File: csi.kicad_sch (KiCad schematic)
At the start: 18 parts, among them J8 Conn_FFC_WE_68712614522_ONE-S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, U11 AP22615A_TSOT26, U12 AP22615A_TSOT26

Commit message: [#54617] Review requested changes
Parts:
- U11, U12: MPN AP22615AWU-7 -> AP22615AWU-7
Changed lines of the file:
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@@
       (effects (font (size 1.27 1.27) (thickness 0.15)) (justify left bottom) hide)
     )
-    (property "Datasheet" " " (at 322.58 171.45 0)
+    (property "Datasheet" "https://product.tdk.com/en/search/capacitor/ceramic/mlcc/info?part_no=C1005X6S1A105K050BC" (at 322.58 171.45 0)
       (effects (font (size 1.27 1.27) (thickness 0.15)) (justify left bottom) hide)
     )
@@
       (effects (font (size 1.27 1.27) (thickness 0.15)) (justify left bottom) hide)
     )
-    (property "Datasheet" "https://search.murata.co.jp/Ceramy/image/img/A01X/G101/ENG/GRM155R61H104KE14-01.pdf" (at 125.73 185.42 0)
+    (property "Datasheet" "https://www.murata.com/products/productdetail?partno=GRM155R61H104KE14%23" (at 125.73 185.42 0)
       (effects (font (size 1.27 1.27) (thickness 0.15)) (justify left bottom) hide)
     )
@@
   (symbol (lib_id "antmicropower:GND") (at 110.49 127 0) (mirror y) (unit 1)
     (in_bom yes) (on_board yes) (dnp no)
-    (property "Reference" "#PWR?" (at 110.49 133.35 0)
+    (property "Reference" "#PWR0217" (at 110.49 133.35 0)
       (effects (font (size 1.27 1.27)) (justify left bottom) hide)
     )
@@
       (project "cm4-baseboard"
         (path "/60b842dc-0853-4a25-99ac-5784ddf94d0d/49e0afda-d892-4d16-b8c1-dc5863c48dfa"
-          (reference "#PWR?") (unit 1)
+          (reference "#PWR0217") (unit 1)
         )
       )
@@
       (effects (font (size 1.27 1.27) (thickness 0.15)) (justify left bottom) hide)
     )
-    (property "Datasheet" "https://search.murata.co.jp/Ceramy/image/img/A01X/G101/ENG/GRM155R61H104KE14-01.pdf" (at 125.73 140.97 0)
+    (property "Datasheet" "https://www.murata.com/products/productdetail?partno=GRM155R61H104KE14%23" (at 125.73 140.97 0)
       (effects (font (size 1.27 1.27) (thickness 0.15)) (justify left bottom) hide)
     )
@@
   (symbol (lib_id "antmicropower:GND") (at 110.49 171.45 0) (mirror y) (unit 1)
     (in_bom yes) (on_board yes) (dnp no)
-    (property "Reference" "#PWR?" (at 110.49 177.8 0)
+    (property "Reference" "#PWR0215" (at 110.49 177.8 0)
       (effects (font (size 1.27 1.27)) (justify left bottom) hide)
     )
@@
       (project "cm4-baseboard"
         (path "/60b842dc-0853-4a25-99ac-5784ddf94d0d/49e0afda-d892-4d16-b8c1-dc5863c48dfa"
-          (reference "#PWR?") (unit 1)
+          (reference "#PWR0215") (unit 1)
         )
       )
@@
       (effects (font (size 1.27 1.27) (thickness 0.15)) (justify left bottom) hide)
     )
-    (property "Datasheet" " " (at 314.96 171.45 0)
+    (property "Datasheet" "https://product.tdk.com/en/search/capacitor/ceramic/mlcc/info?part_no=C1005X6S1A105K050BC" (at 314.96 171.45 0)
       (effects (font (size 1.27 1.27) (thickness 0.15)) (justify left bottom) hide)
     )
@@
       (effects (font (size 1.27 1.27) (thickness 0.15)) (justify left bottom) hide)
     )
-    (property "Datasheet" "https://www.mouser.pl/datasheet/2/115/DIOD_S_A0008958405_1-2543193.pdf" (at 152.4 139.7 0)
-      (effects (font (size 1.27 1.27) (thickness 0.15)) (justify left bottom) hide)
-    )
-    (property "MPN" "AP22615AWU-7 " (at 129.54 125.73 0)
+    (property "Datasheet" "https://www.mouser.com/datasheet/2/115/DIOD_S_A0008958405_1-2543193.pdf" (at 152.4 139.7 0)
+      (effects (font (size 1.27 1.27) (thickness 0.15)) (justify left bottom) hide)
+    )
+    (property "MPN" "AP22615AWU-7" (at 129.54 125.73 0)
       (effects (font (size 1.27 1.27) (thickness 0.15)))
     )
@@
   (symbol (lib_id "antmicropower:+3V3") (at 110.49 162.56 0) (unit 1)
     (in_bom yes) (on_board yes) (dnp no)
-    (property "Reference" "#PWR?" (at 110.49 166.37 0)
+    (property "Reference" "#PWR0216" (at 110.49 166.37 0)
       (effects (font (size 1.27 1.27)) (justify left bottom) hide)
     )
@@
       (effects (font (size 1.27 1.27)) hide)
     )
-    (pin "1")
-    (instances
-      (project "cm4-baseboard"
-        (path "/60b842dc-0853-4a25-99ac-5784ddf94d0d/49e0afda-d892-4d16-b8c1-dc5863c48dfa"
-          (reference "#PWR?") (unit 1)
+    (property "Author" "Antmicro" (at 125.73 165.1 0)
+      (effects (font (size 1.27 1.27) (thickness 0.15)) (justify left bottom) hide)
+    )
+    (property "License" "Apache-2.0" (at 125.73 167.64 0)
+      (effects (font (size 1.27 1.27) (thickness 0.15)) (justify left bottom) hide)
+    )
+    (pin "1")
+    (instances
+      (project "cm4-baseboard"
+        (path "/60b842dc-0853-4a25-99ac-5784ddf94d0d/49e0afda-d892-4d16-b8c1-dc5863c48dfa"
+          (reference "#PWR0216") (unit 1)
         )
       )
@@
       (effects (font (size 1.27 1.27) (thickness 0.15)) (justify left bottom) hide)
     )
-    (property "Datasheet" "https://www.mouser.pl/datasheet/2/115/DIOD_S_A0008958405_1-2543193.pdf" (at 152.4 184.15 0)
-      (effects (font (size 1.27 1.27) (thickness 0.15)) (justify left bottom) hide)
-    )
-    (property "MPN" "AP22615AWU-7 " (at 129.54 170.18 0)
+    (property "Datasheet" "https://www.mouser.com/datasheet/2/115/DIOD_S_A0008958405_1-2543193.pdf" (at 152.4 184.15 0)
+      (effects (font (size 1.27 1.27) (thickness 0.15)) (justify left bottom) hide)
+    )
+    (property "MPN" "AP22615AWU-7" (at 129.54 170.18 0)
       (effects (font (size 1.27 1.27) (thickness 0.15)))
     )
@@
       (effects (font (size 1.27 1.27)) hide)
     )
-    (pin "1")
+    (property "Author" "Antmicro" (at 125.73 125.73 0)
+      (effects (font (size 1.27 1.27) (thickness 0.15)) (justify left bottom) hide)
+    )
+    (property "License" "Apache-2.0" (at 125.73 128.27 0)
+      (effects (font (size 1.27 1.27) (thickness 0.15)) (justify left bottom) hide)
+    )
+    (pin "1")

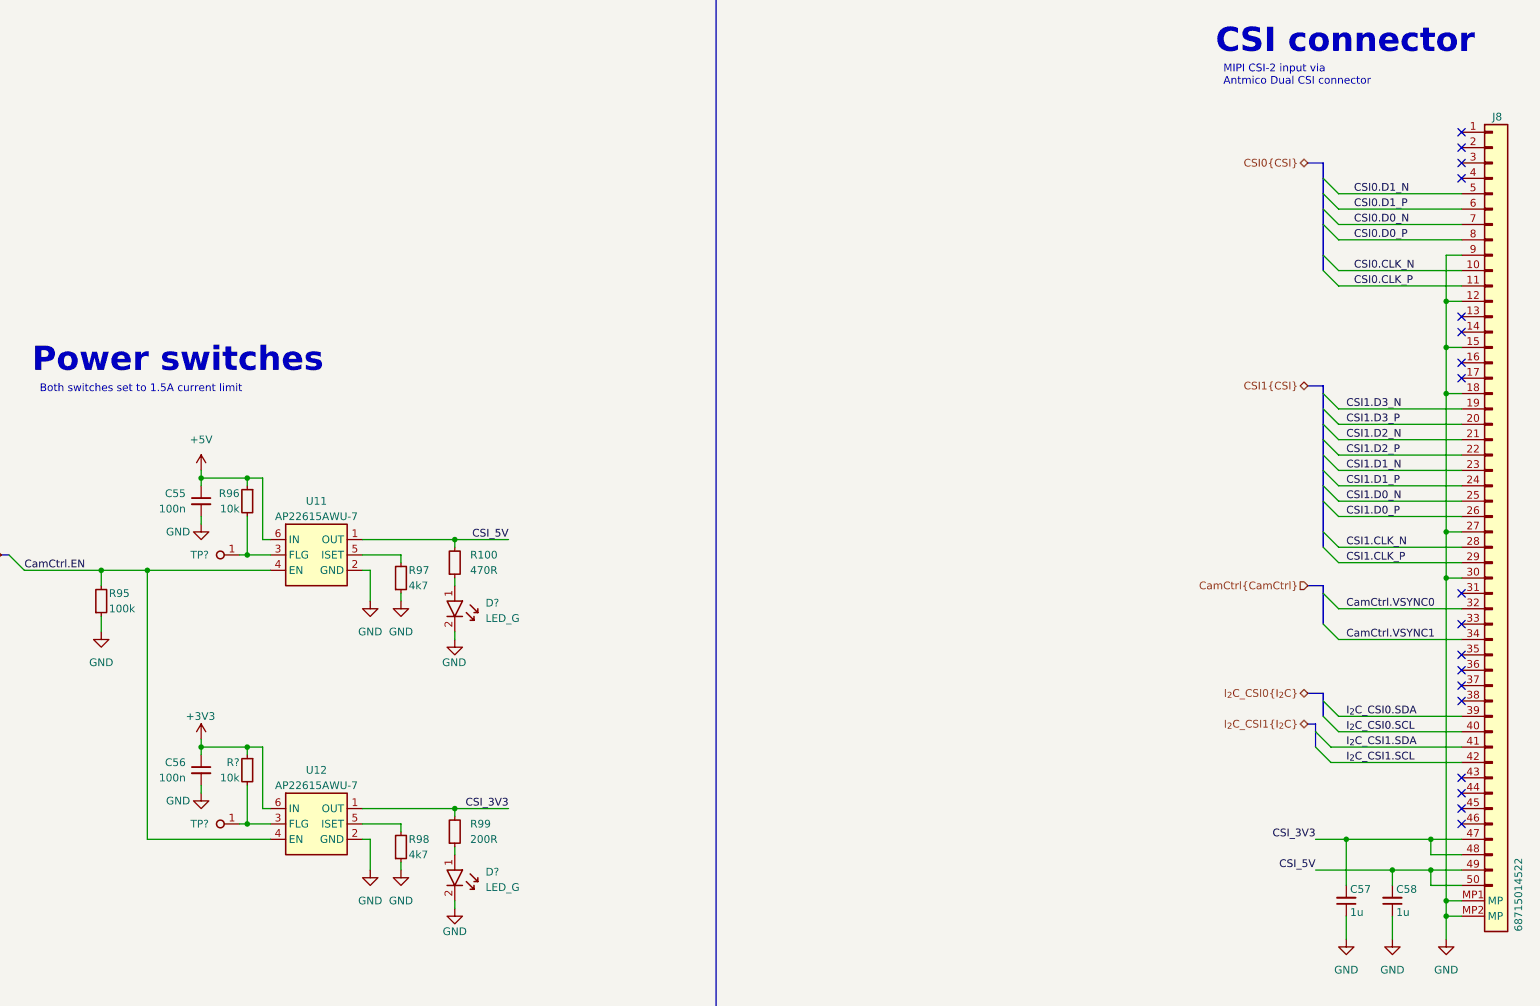
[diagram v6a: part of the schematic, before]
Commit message: [#54617] Re-enumerate reference designators
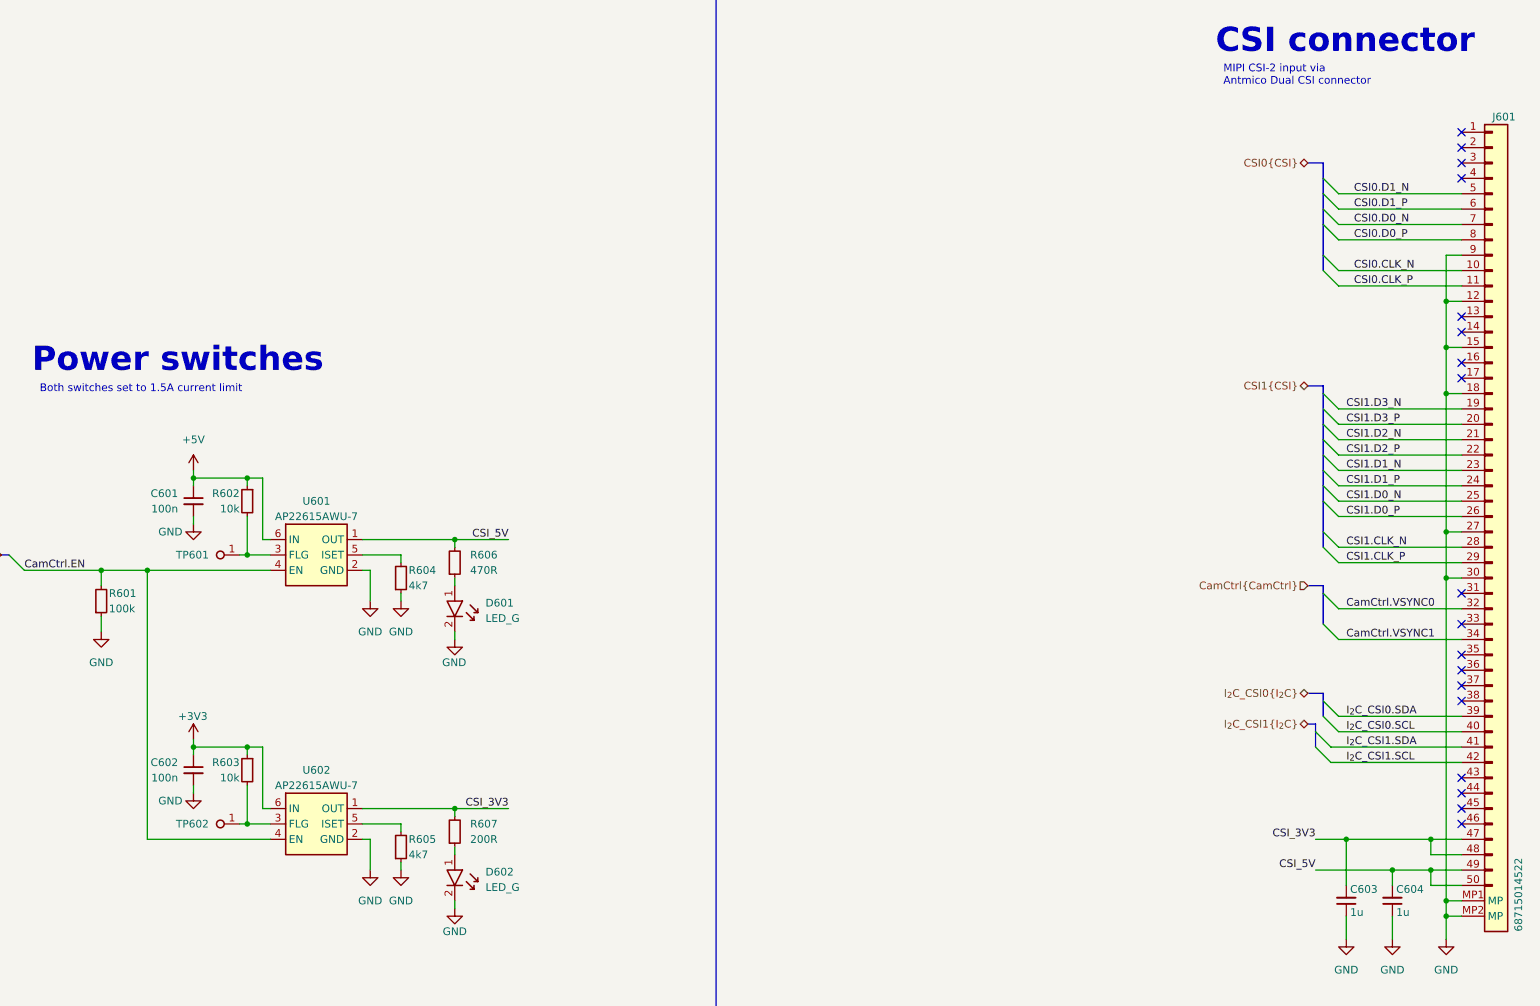
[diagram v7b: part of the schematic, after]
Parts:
- gave numbers to parts that had none: 5
- renumbered C55 to C601, C56 to C602, C57 to C603, C58 to C604, J8 to J601, R95 to R601, R96 to R602, R97 to R604, R98 to R605, R100 to R606, R99 to R607, U11 to U601, U12 to U602
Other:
- moved on the sheet: C601, C602

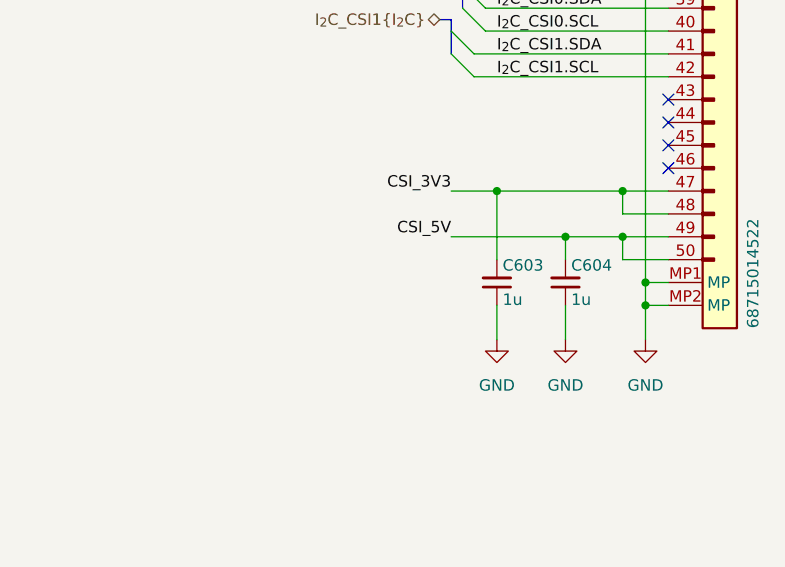
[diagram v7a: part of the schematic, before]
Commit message: [#55247] Change USB schematic: Remove PD from App USB, add CC controller
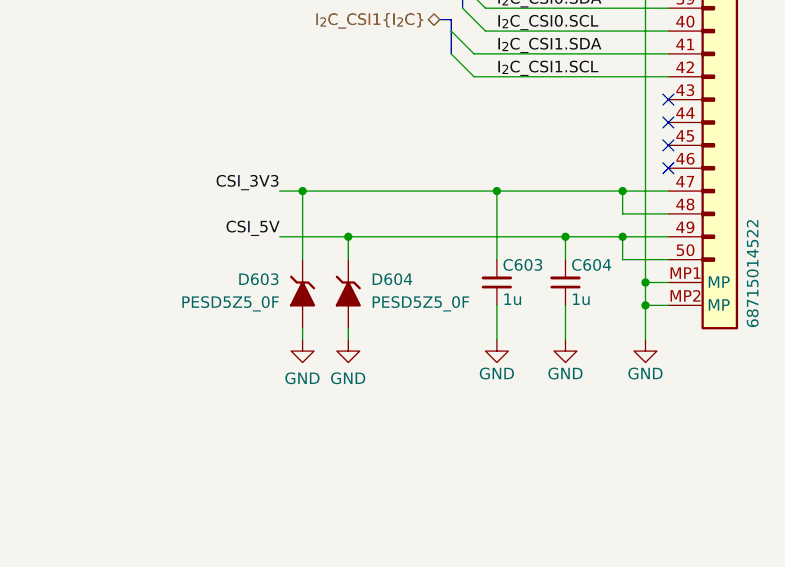
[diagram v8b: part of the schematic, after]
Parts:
- added D603, D604: PESD5Z5_0F, antmicro-footprints:SOD-523, symbol antmicroTVSDiodes:PESD5Z5_0F
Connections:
- net CSI_3V3: now also D603.1
- net CSI_5V: now also D604.1
- net GND: now also D603.2, D604.2
